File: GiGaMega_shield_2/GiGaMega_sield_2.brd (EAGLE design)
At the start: 130.7 x 81.8 mm, 34 parts

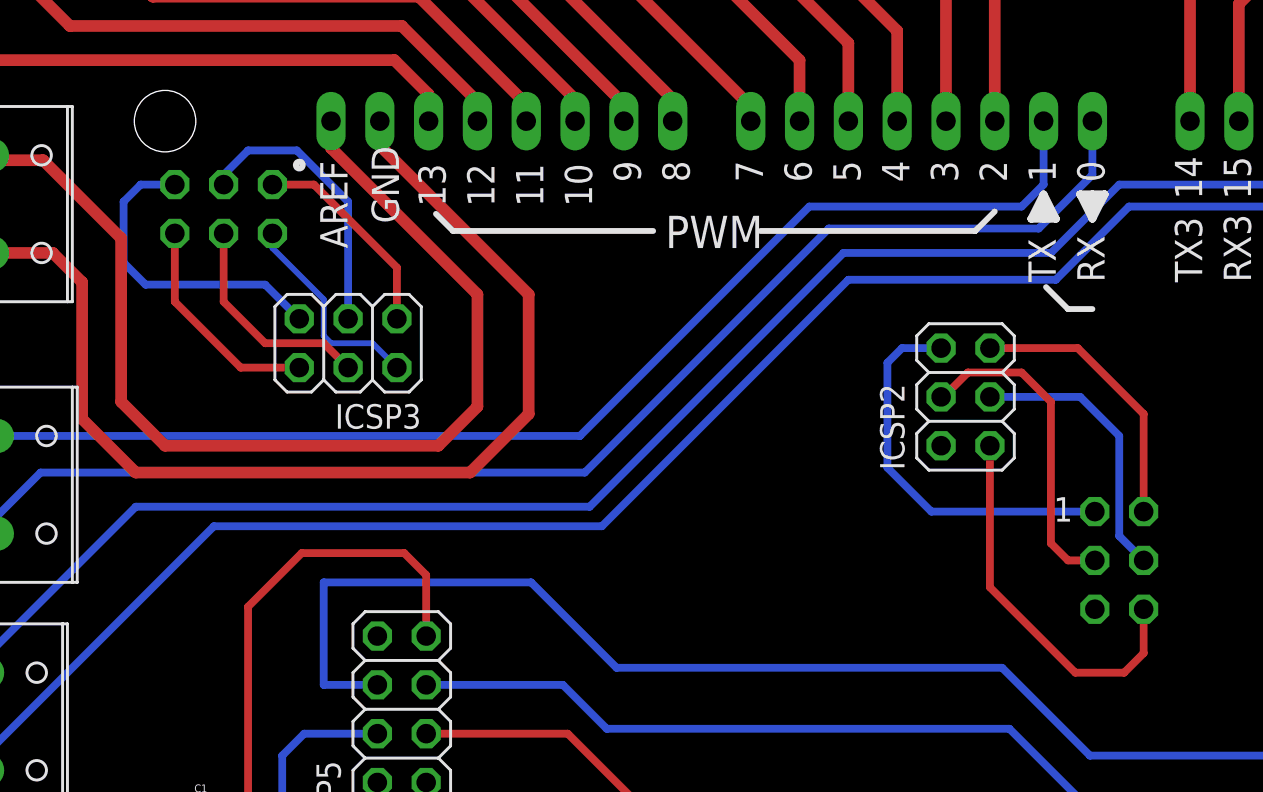
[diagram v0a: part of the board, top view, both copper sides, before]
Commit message: Correct SPI connectors
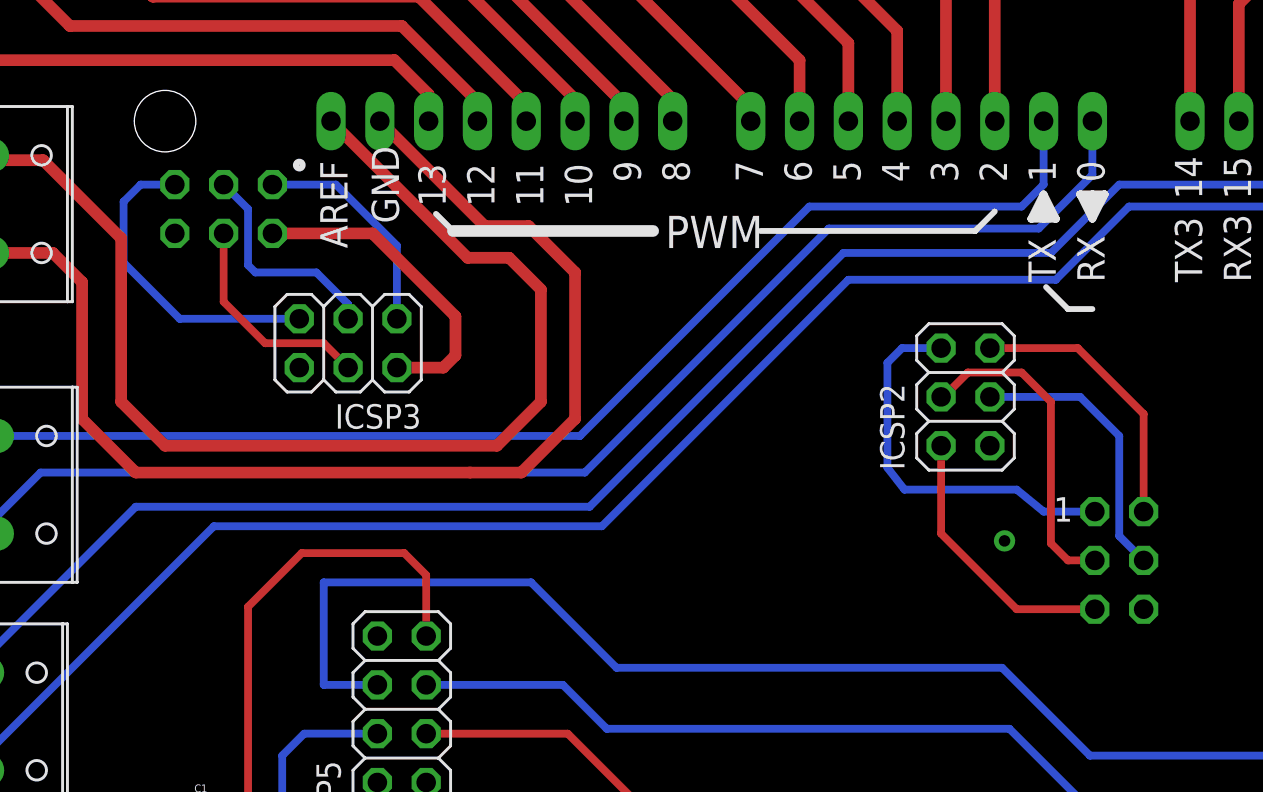
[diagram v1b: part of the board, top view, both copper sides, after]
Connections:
- removed net N$17 (its old number): ICSP.5, ICSP2.1
- removed net N$22: ICSP1.2, ICSP3.6
- new net N$20: ICSP1.6, ICSP3.2
- new net N$21: ICSP.6, ICSP2.2
- net GND: now also ICSP.5, ICSP1.2, ICSP2.1, ICSP3.6; no longer ICSP.6, ICSP1.6, ICSP2.2, ICSP3.2
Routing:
- net N$17 (its old number): track 19.9 -> 0.00 mm
- net N$20: track 0.00 -> 16.7 mm
- net N$21: track 0.00 -> 14.2 mm
- net N$22: track 11.5 -> 0.00 mm
- net GND: track 10.9 -> 0.00 mm, vias 1 -> 2
- net N$36: track 56.3 -> 62.0 mm
- net N$35: track 57.4 -> 62.3 mm
- net N$2: track 14.7 -> 11.5 mm
- net N$17: track 10.9 -> 11.6 mm
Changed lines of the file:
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@@
 <wire x1="46.228" y1="45.085" x2="57.404" y2="45.085" width="0.3048" layer="21"/>
 <wire x1="57.404" y1="45.085" x2="58.42" y2="46.101" width="0.3048" layer="21"/>
-<wire x1="40.64" y1="45.085" x2="30.226" y2="45.085" width="0.3048" layer="21"/>
+<wire x1="40.64" y1="45.085" x2="30.226" y2="45.085" width="0.6096" layer="21"/>
 <wire x1="30.226" y1="45.085" x2="29.337" y2="45.974" width="0.3048" layer="21"/>
 <wire x1="61.087" y1="42.164" x2="62.23" y2="41.021" width="0.3048" layer="21"/>
@@
 <contactref element="C1" pad="1"/>
 <via x="13.335" y="10.922" extent="1-16" drill="0.8" diameter="2.1844" shape="octagon"/>
-<contactref element="ICSP2" pad="2"/>
-<contactref element="ICSP" pad="6"/>
-<contactref element="ICSP1" pad="6"/>
-<contactref element="ICSP3" pad="2"/>
-<wire x1="20.828" y1="44.958" x2="20.828" y2="44.196" width="0.3048" layer="16"/>
-<wire x1="20.828" y1="44.196" x2="23.495" y2="41.529" width="0.3048" layer="16"/>
-<wire x1="23.495" y1="41.529" x2="23.495" y2="39.624" width="0.3048" layer="16"/>
-<wire x1="23.495" y1="39.624" x2="23.876" y2="39.243" width="0.3048" layer="16"/>
-<wire x1="23.876" y1="39.243" x2="26.035" y2="39.243" width="0.3048" layer="16"/>
-<wire x1="26.035" y1="39.243" x2="27.305" y2="37.973" width="0.3048" layer="16"/>
+<contactref element="ICSP2" pad="1"/>
+<contactref element="ICSP" pad="5"/>
+<contactref element="ICSP3" pad="6"/>
+<contactref element="ICSP1" pad="2"/>
+<via x="58.928" y="28.956" extent="1-16" drill="0.6" shape="square"/>
 </signal>
 <signal name="RESET">
@@
 <wire x1="64.897" y1="29.21" x2="66.167" y2="27.94" width="0.4064" layer="16"/>
 </signal>
-<signal name="N$17">
-<contactref element="ICSP2" pad="1"/>
-<contactref element="ICSP" pad="5"/>
-<wire x1="58.166" y1="33.909" x2="58.166" y2="26.543" width="0.4064" layer="1"/>
-<wire x1="58.166" y1="26.543" x2="62.611" y2="22.098" width="0.4064" layer="1"/>
-<wire x1="62.611" y1="22.098" x2="65.151" y2="22.098" width="0.4064" layer="1"/>
-<wire x1="65.151" y1="22.098" x2="66.167" y2="23.114" width="0.4064" layer="1"/>
-<wire x1="66.167" y1="23.114" x2="66.167" y2="25.4" width="0.4064" layer="1"/>
-</signal>
 <signal name="N$18">
 <contactref element="ICSP2" pad="6"/>
@@
 <wire x1="55.626" y1="38.989" x2="53.594" y2="38.989" width="0.4064" layer="16"/>
 <wire x1="53.594" y1="38.989" x2="52.832" y2="38.227" width="0.4064" layer="16"/>
-<wire x1="52.832" y1="38.227" x2="52.832" y2="32.766" width="0.4064" layer="16"/>
-<wire x1="52.832" y1="32.766" x2="55.118" y2="30.48" width="0.4064" layer="16"/>
-<wire x1="55.118" y1="30.48" x2="63.627" y2="30.48" width="0.4064" layer="16"/>
+<wire x1="52.832" y1="32.766" x2="52.832" y2="38.227" width="0.4064" layer="16"/>
+<wire x1="63.627" y1="30.48" x2="60.96" y2="30.48" width="0.4064" layer="16"/>
+<wire x1="60.96" y1="30.48" x2="59.563" y2="31.623" width="0.4064" layer="16"/>
+<wire x1="59.563" y1="31.623" x2="53.721" y2="31.623" width="0.4064" layer="16"/>
+<wire x1="53.721" y1="31.623" x2="52.832" y2="32.766" width="0.4064" layer="16"/>
 </signal>
 <signal name="N$19">
@@
 <wire x1="15.748" y1="47.498" x2="13.97" y2="47.498" width="0.4064" layer="16"/>
 <wire x1="13.97" y1="47.498" x2="13.081" y2="46.609" width="0.4064" layer="16"/>
-<wire x1="13.081" y1="46.609" x2="13.081" y2="43.434" width="0.4064" layer="16"/>
-<wire x1="13.081" y1="43.434" x2="14.224" y2="42.291" width="0.4064" layer="16"/>
-<wire x1="14.224" y1="42.291" x2="20.447" y2="42.291" width="0.4064" layer="16"/>
-<wire x1="20.447" y1="42.291" x2="22.225" y2="40.513" width="0.4064" layer="16"/>
+<wire x1="13.081" y1="43.434" x2="13.081" y2="46.609" width="0.4064" layer="16"/>
+<wire x1="22.225" y1="40.513" x2="16.002" y2="40.513" width="0.4064" layer="16"/>
+<wire x1="16.002" y1="40.513" x2="13.081" y2="43.434" width="0.4064" layer="16"/>
 </signal>
 <signal name="N$2">
 <contactref element="ICSP1" pad="3"/>
 <contactref element="ICSP3" pad="3"/>
-<wire x1="18.288" y1="47.498" x2="18.288" y2="48.006" width="0.4064" layer="16"/>
-<wire x1="18.288" y1="48.006" x2="19.558" y2="49.276" width="0.4064" layer="16"/>
-<wire x1="19.558" y1="49.276" x2="22.098" y2="49.276" width="0.4064" layer="16"/>
-<wire x1="22.098" y1="49.276" x2="24.765" y2="46.609" width="0.4064" layer="16"/>
-<wire x1="24.765" y1="46.609" x2="24.765" y2="40.513" width="0.4064" layer="16"/>
-</signal>
-<signal name="N$21">
-<contactref element="ICSP1" pad="5"/>
-<contactref element="ICSP3" pad="1"/>
-<wire x1="20.828" y1="47.498" x2="22.987" y2="47.498" width="0.4064" layer="1"/>
-<wire x1="22.987" y1="47.498" x2="27.305" y2="43.18" width="0.4064" layer="1"/>
-<wire x1="27.305" y1="43.18" x2="27.305" y2="40.513" width="0.4064" layer="1"/>
-</signal>
-<signal name="N$22">
-<contactref element="ICSP3" pad="6"/>
-<contactref element="ICSP1" pad="2"/>
-<wire x1="15.748" y1="44.958" x2="15.748" y2="41.402" width="0.4064" layer="1"/>
-<wire x1="15.748" y1="41.402" x2="19.177" y2="37.973" width="0.4064" layer="1"/>
-<wire x1="19.177" y1="37.973" x2="22.225" y2="37.973" width="0.4064" layer="1"/>
+<wire x1="24.765" y1="40.513" x2="24.765" y2="41.275" width="0.4064" layer="16"/>
+<wire x1="24.765" y1="41.275" x2="23.114" y2="42.926" width="0.4064" layer="16"/>
+<wire x1="23.114" y1="42.926" x2="19.939" y2="42.926" width="0.4064" layer="16"/>
+<wire x1="19.939" y1="42.926" x2="19.558" y2="43.307" width="0.4064" layer="16"/>
+<wire x1="19.558" y1="43.307" x2="19.558" y2="46.228" width="0.4064" layer="16"/>
+<wire x1="19.558" y1="46.228" x2="18.288" y2="47.498" width="0.4064" layer="16"/>
 </signal>
 <signal name="N$23">
@@
 <contactref element="PWMH" pad="2"/>
 <contactref element="X5" pad="2"/>
-<wire x1="26.416" y1="50.8" x2="26.416" y2="49.53" width="0.6096" layer="1"/>
-<wire x1="26.416" y1="49.53" x2="34.163" y2="41.783" width="0.6096" layer="1"/>
-<wire x1="34.163" y1="41.783" x2="34.163" y2="35.56" width="0.6096" layer="1"/>
-<wire x1="34.163" y1="35.56" x2="31.115" y2="32.512" width="0.6096" layer="1"/>
-<wire x1="31.115" y1="32.512" x2="13.716" y2="32.512" width="0.6096" layer="1"/>
+<wire x1="13.716" y1="32.512" x2="31.115" y2="32.512" width="0.6096" layer="1"/>
 <wire x1="13.716" y1="32.512" x2="10.922" y2="35.306" width="0.6096" layer="1"/>
 <wire x1="10.922" y1="35.306" x2="10.922" y2="42.418" width="0.6096" layer="1"/>
 <wire x1="10.922" y1="42.418" x2="9.398" y2="43.942" width="0.6096" layer="1"/>
 <wire x1="9.398" y1="43.942" x2="5.334" y2="43.942" width="0.6096" layer="1"/>
+<wire x1="31.115" y1="32.512" x2="33.782" y2="32.512" width="0.6096" layer="1"/>
+<wire x1="33.782" y1="32.512" x2="36.576" y2="35.306" width="0.6096" layer="1"/>
+<wire x1="36.576" y1="35.306" x2="36.576" y2="42.926" width="0.6096" layer="1"/>
+<wire x1="36.576" y1="42.926" x2="34.163" y2="45.339" width="0.6096" layer="1"/>
+<wire x1="34.163" y1="45.339" x2="31.877" y2="45.339" width="0.6096" layer="1"/>
+<wire x1="31.877" y1="45.339" x2="26.416" y2="50.8" width="0.6096" layer="1"/>
 </signal>
 <signal name="N$36">
 <contactref element="PWMH" pad="1"/>
 <contactref element="X5" pad="1"/>
-<wire x1="23.876" y1="50.8" x2="23.876" y2="49.403" width="0.6096" layer="1"/>
-<wire x1="23.876" y1="49.403" x2="31.496" y2="41.783" width="0.6096" layer="1"/>
-<wire x1="31.496" y1="41.783" x2="31.496" y2="35.941" width="0.6096" layer="1"/>
-<wire x1="31.496" y1="35.941" x2="29.464" y2="33.909" width="0.6096" layer="1"/>
-<wire x1="29.464" y1="33.909" x2="15.24" y2="33.909" width="0.6096" layer="1"/>
-<wire x1="15.24" y1="33.909" x2="12.954" y2="36.195" width="0.6096" layer="1"/>
+<wire x1="12.954" y1="36.195" x2="15.24" y2="33.909" width="0.6096" layer="1"/>
 <wire x1="12.954" y1="36.195" x2="12.954" y2="44.704" width="0.6096" layer="1"/>
 <wire x1="12.954" y1="44.704" x2="8.89" y2="48.768" width="0.6096" layer="1"/>
 <wire x1="8.89" y1="48.768" x2="5.588" y2="48.768" width="0.6096" layer="1"/>
 <wire x1="5.588" y1="48.768" x2="5.334" y2="49.022" width="0.6096" layer="1"/>
+<wire x1="32.512" y1="33.909" x2="34.798" y2="36.195" width="0.6096" layer="1"/>
+<wire x1="34.798" y1="36.195" x2="34.798" y2="42.037" width="0.6096" layer="1"/>
+<wire x1="34.798" y1="42.037" x2="33.147" y2="43.688" width="0.6096" layer="1"/>
+<wire x1="33.147" y1="43.688" x2="30.988" y2="43.688" width="0.6096" layer="1"/>
+<wire x1="30.988" y1="43.688" x2="23.876" y2="50.8" width="0.6096" layer="1"/>
+<wire x1="15.24" y1="33.909" x2="32.512" y2="33.909" width="0.6096" layer="1"/>
 </signal>
 <signal name="N$9">
@@
 <wire x1="87.503" y1="15.24" x2="93.98" y2="15.24" width="0.4064" layer="16"/>
 </signal>
+<signal name="N$20">
+<contactref element="ICSP3" pad="2"/>
+<contactref element="ICSP1" pad="6"/>
+<wire x1="27.305" y1="37.973" x2="29.718" y2="37.973" width="0.6096" layer="1"/>
+<wire x1="29.718" y1="37.973" x2="30.353" y2="38.608" width="0.6096" layer="1"/>
+<wire x1="30.353" y1="38.608" x2="30.353" y2="40.64" width="0.6096" layer="1"/>
+<wire x1="30.353" y1="40.64" x2="26.035" y2="44.958" width="0.6096" layer="1"/>
+<wire x1="26.035" y1="44.958" x2="20.828" y2="44.958" width="0.6096" layer="1"/>
+</signal>
+<signal name="N$21">
+<contactref element="ICSP2" pad="2"/>
+<contactref element="ICSP" pad="6"/>
+<wire x1="55.626" y1="33.909" x2="55.626" y2="29.337" width="0.4064" layer="1"/>
+<wire x1="55.626" y1="29.337" x2="59.563" y2="25.4" width="0.4064" layer="1"/>
+<wire x1="59.563" y1="25.4" x2="63.627" y2="25.4" width="0.4064" layer="1"/>
+</signal>
+<signal name="N$17">
+<contactref element="ICSP1" pad="5"/>
+<contactref element="ICSP3" pad="1"/>
+<wire x1="27.305" y1="40.513" x2="27.305" y2="44.323" width="0.4064" layer="16"/>
+<wire x1="27.305" y1="44.323" x2="24.13" y2="47.498" width="0.4064" layer="16"/>
+<wire x1="24.13" y1="47.498" x2="20.828" y2="47.498" width="0.4064" layer="16"/>
+</signal>
 </signals>
